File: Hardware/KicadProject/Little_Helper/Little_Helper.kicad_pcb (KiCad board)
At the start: 4 copper layers, 84 x 19.6 mm, 1 part, among them U1 ESP32-S3-MINI-1

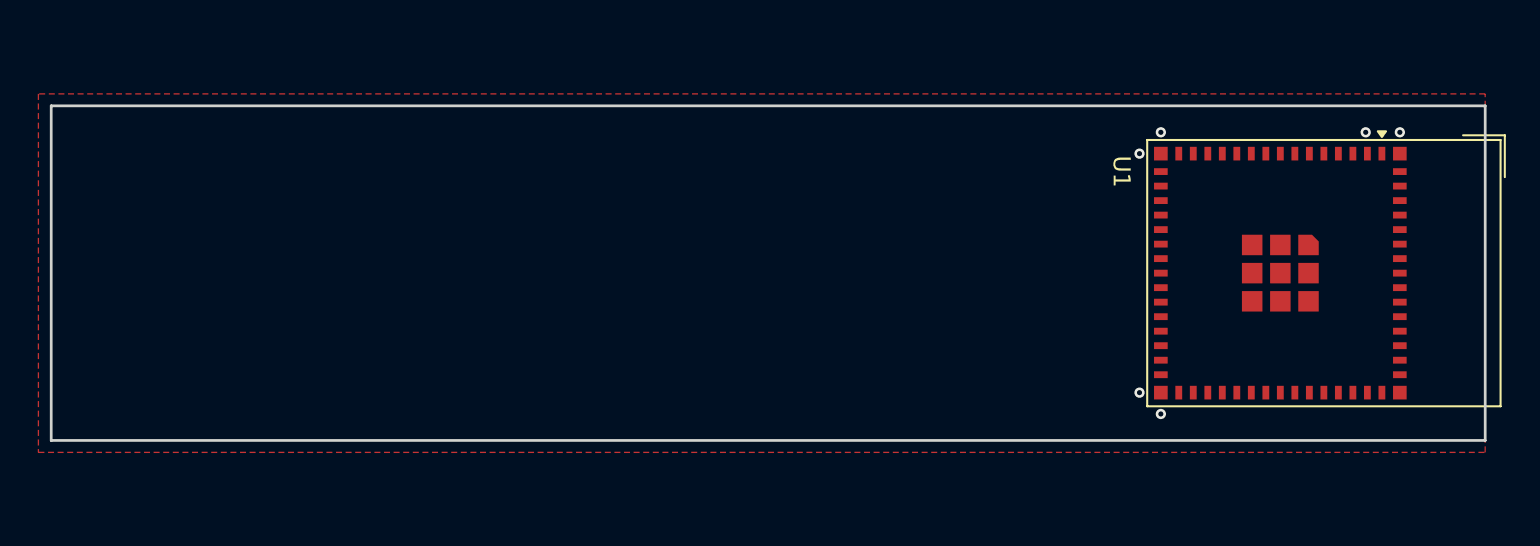
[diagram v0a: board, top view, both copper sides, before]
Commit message: fix some library mismatch
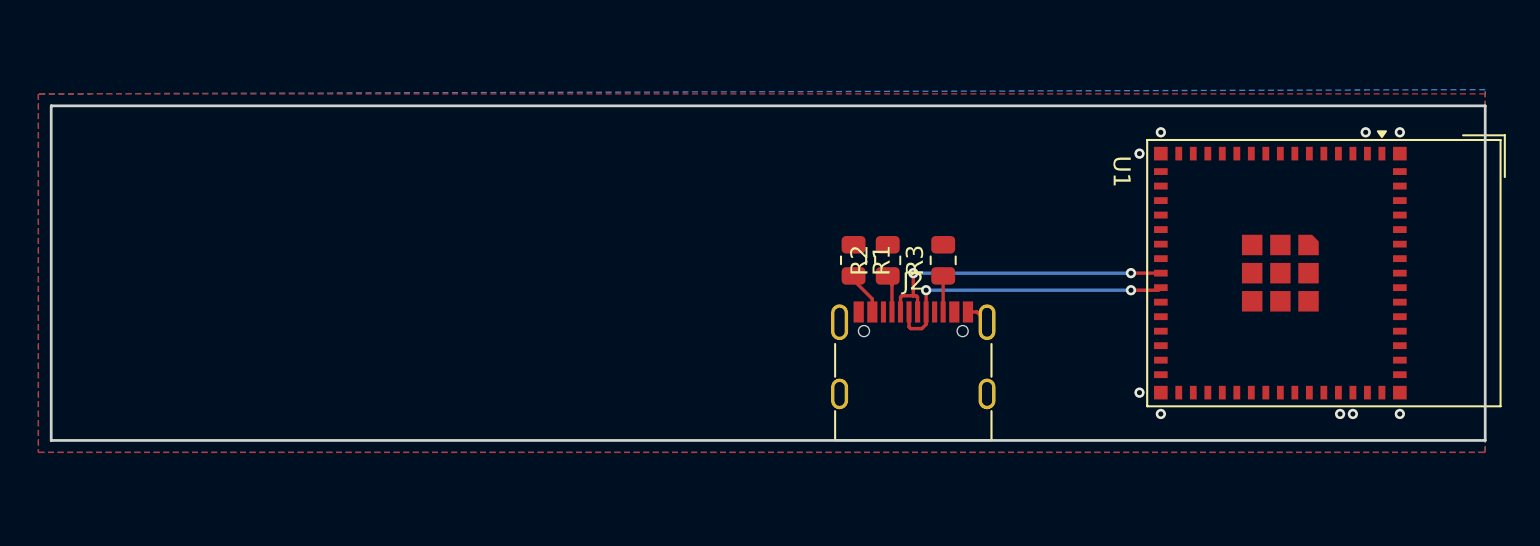
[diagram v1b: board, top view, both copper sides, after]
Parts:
- added J2: USB_C_Receptacle_USB2.0_16P, Connector_USB:USB_C_Receptacle_G-Switch_GT-USB-7010ASV, F.Cu at (8.50, 6.00)
- added R1: 100k, Resistor_SMD:R_0805_2012Metric, F.Cu at (5.00, -0.75)
- added R2: 5k1, Resistor_SMD:R_0805_2012Metric, F.Cu at (7.00, -0.75)
- added R3: 5k1, Resistor_SMD:R_0805_2012Metric, F.Cu at (10.2, -0.75)
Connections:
- U1 pad 23: unconnected-(U1-IO19-Pad23) -> /Usb_D-
- U1 pad 24: unconnected-(U1-IO20-Pad24) -> /Usb_D+
- U1 pad 3: unconnected-(U1-3V3-Pad3) -> +3.3V
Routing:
- net /Usb_D-: track 0.00 -> 18.6 mm, vias 0 -> 2
- net /Usb_D+: track 0.00 -> 17.8 mm, vias 0 -> 2
- net VBUS: track 0.00 -> 2.32 mm
- net Net-(J2-CC2): track 0.00 -> 2.11 mm
- net Net-(J2-CC1): track 0.00 -> 1.97 mm
- net GND: track 0.00 -> 1.37 mm, vias 6 -> 9
- added copper zone on B.Cu, net GND

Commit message: add tactile buttons
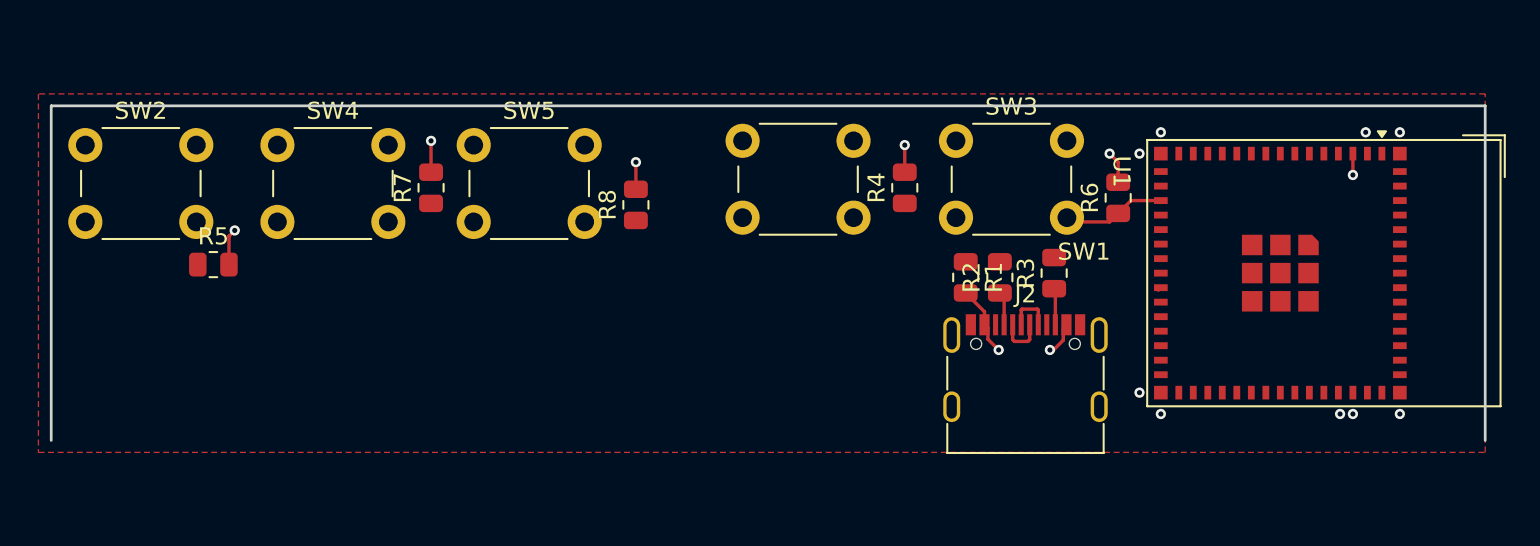
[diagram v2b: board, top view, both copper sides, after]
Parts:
- added R4: 10k, Resistor_SMD:R_0805_2012Metric, F.Cu at (8.00, -5.00)
- added R5: 10k, Resistor_SMD:R_0805_2012Metric, F.Cu at (-32.5, -0.50)
- added R6: 10k, Resistor_SMD:R_0805_2012Metric, F.Cu at (20.5, -4.41)
- added R7: 10k, Resistor_SMD:R_0805_2012Metric, F.Cu at (-19.8, -5.00)
- added R8: 10k, Resistor_SMD:R_0805_2012Metric, F.Cu at (-7.75, -4.00)
- added SW1: SW_Push, Button_Switch_THT:SW_PUSH_6mm_H5mm, F.Cu at (5.00, -3.25)
- added SW2: SW_Push, Button_Switch_THT:SW_PUSH_6mm_H5mm, F.Cu at (-40.0, -7.50)
- added SW3: SW_Push, Button_Switch_THT:SW_PUSH_6mm_H5mm, F.Cu at (11.0, -7.75)
- added SW4: SW_Push, Button_Switch_THT:SW_PUSH_6mm_H5mm, F.Cu at (-28.8, -7.50)
- added SW5: SW_Push, Button_Switch_THT:SW_PUSH_6mm_H5mm, F.Cu at (-17.2, -7.50)
- moved R1 6.65 mm to (11.6, 0.25)
- moved R2 6.65 mm to (13.6, 0.25)
- moved J2 6.61 mm to (15.1, 6.75)
- moved R3 6.54 mm to (16.8, 0.00)
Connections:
- U1 pad 14: unconnected-(U1-IO10-Pad14) -> /BTN_1_RV
- U1 pad 15: unconnected-(U1-IO11-Pad15) -> /BTN_1_STOP
- U1 pad 16: unconnected-(U1-IO12-Pad16) -> /BTN_1_VW
- U1 pad 17: unconnected-(U1-IO13-Pad17) -> /BTN_1_REC
- U1 pad 18: unconnected-(U1-IO14-Pad18) -> /BTN_1_PL
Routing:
- net /Usb_D-: track 18.6 -> 2.83 mm, vias 2 -> 0
- net /Usb_D+: track 17.8 -> 2.99 mm, vias 2 -> 0
- net +3.3V: track 0.00 -> 10.3 mm, vias 0 -> 6
- net /BTN_1_PL: track 0.00 -> 6.41 mm
- net VBUS: track 2.32 -> 6.14 mm, vias 0 -> 2
- net GND: track 1.37 -> 0.00 mm
- added copper zone on In2.Cu, net +3.3V
- added copper zone on In2.Cu, net VBUS
- removed copper zone on B.Cu, net GND

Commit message: board in progress
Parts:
- removed the R3 at (16.8, 0.00)
- added C1: 10uF, Capacitor_SMD:C_0603_1608Metric, F.Cu at (-3.00, -0.10)
- added C2: 10uF, Capacitor_SMD:C_0603_1608Metric, F.Cu at (32.6, -9.60)
- added C3: 10uF, Capacitor_SMD:C_0603_1608Metric, F.Cu at (-7.80, 1.30)
- added C4: 10uF, Capacitor_SMD:C_0603_1608Metric, F.Cu at (-18.1, 7.20)
- added C5: 10uF, Capacitor_SMD:C_0603_1608Metric, F.Cu at (29.4, -9.57)
- added C6: 10uF, Capacitor_SMD:C_0603_1608Metric, F.Cu at (31.0, -9.57)
- added C7: 1uF, Capacitor_SMD:C_0603_1608Metric, F.Cu at (34.2, -9.62)
- added C8: 10uF, Capacitor_SMD:C_0603_1608Metric, F.Cu at (-8.10, 8.40)
- added C9: 1uF, Capacitor_SMD:C_0603_1608Metric, F.Cu at (25.3, 8.80)
- added D1: MBR0540, Diode_SMD:D_0805_2012Metric, F.Cu at (-14.6, 9.60)
- added D2: LED, LED_SMD:LED_0603_1608Metric, F.Cu at (-11.3, 7.00)
- added D3: WS2812B, LED_SMD:LED_WS2812B_PLCC4_5.0x5.0mm_P3.2mm, F.Cu at (-25.1, 2.00)
- added D4: BAS16, ba_sot:sot_23, F.Cu at (-11.7, 0.20)
- added J2: Conn_01x02_Pin, Connector_Hirose:Hirose_DF13-02P-1.25DSA_1x02_P1.25mm_Vertical, B.Cu at (-36.9, 8.30)
- added Q1: DMG3415U, Package_TO_SOT_SMD:SOT-23, F.Cu at (-18.2, 9.90)
- added R10: 5k1, Resistor_SMD:R_0805_2012Metric, F.Cu at (-11.4, 9.10)
- added R11: 5k1, Resistor_SMD:R_0805_2012Metric, F.Cu at (-4.80, 3.70)
- added R9: 10k, Resistor_SMD:R_0805_2012Metric, F.Cu at (20.5, -4.50)
- added SW6: SW_SPST, Button_Switch_SMD:SW_SPDT_CK_JS102011SAQN, F.Cu at (-26.2, 10.6)
- added SW7: SW_Push, Button_Switch_SMD:SW_Push_1P1T_NO_Vertical_Wuerth_434133025816, F.Cu at (16.5, 7.90)
- added SW8: SW_Push, Button_Switch_SMD:SW_Push_1P1T_NO_Vertical_Wuerth_434133025816, F.Cu at (16.4, 3.70)
- added U1: AP2112K-3.3, Package_TO_SOT_SMD:SOT-23-5, F.Cu at (-11.6, 3.80)
- added U3: MCP73831-2-OT, Package_TO_SOT_SMD:SOT-23-5, F.Cu at (-5.20, 7.60)
- J1: renamed from J2; value USB_C_Receptacle_USB2.0_16P -> USB_B_Micro; footprint Connector_USB:USB_C_Receptacle_G-Switch_GT-USB-7010ASV -> Connector_USB:USB_Micro-B_Wuerth_629105150521_CircularHoles
- R3: renamed from R1; value 100k -> R2012_100K; footprint Resistor_SMD:R_0805_2012Metric -> ba_res:r2012
- R4: value 10k -> 100k
- moved SW1 45.2 mm to (-40.0, -7.75), turned to 0 degrees
- moved R6 40.0 mm to (-19.5, -5.34)
- moved SW5 28.3 mm to (11.0, -7.75)
- moved SW3 28.0 mm to (-17.0, -7.75)
- moved SW4 27.3 mm to (-1.50, -7.75)
- moved R4 24.6 mm to (-15.0, 3.80)
- moved R8 15.8 mm to (8.00, -5.00)
- moved R7 12.0 mm to (-7.75, -4.25)
- moved SW2 11.5 mm to (-28.5, -7.75)
- moved R1 10.6 mm to (20.7, 8.09), turned to -90 degrees
- moved J1 7.98 mm to (7.39, 8.95)
- moved R3 5.99 mm to (6.60, 3.60), turned to 90 degrees
- renumbered R2 to R1, U1 to U2
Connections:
- R1 pad 1: Net-(J2-CC1) -> +3.3V
- R1 pad 2: GND -> /RESET
- R3 pad 1: GND -> VBUS
- R3 pad 2: VBUS -> GND
- R4 pad 1: /BTN_1_REC -> Net-(U1-EN)
- R4 pad 2: +3.3V -> /NEOPIX_VDD
- R6 pad 1: /BTN_1_PL -> /BTN_1_STOP
- R7 pad 1: /BTN_1_STOP -> /BTN_1_VW
- R8 pad 1: /BTN_1_VW -> /BTN_1_REC
- SW1 pad 2: /BTN_1_REC -> /BTN_1_RV
- SW2 pad 2: /BTN_1_RV -> /BTN_1_STOP
- SW3 pad 2: /BTN_1_PL -> /BTN_1_VW
- SW4 pad 2: /BTN_1_STOP -> /BTN_1_REC
- SW5 pad 2: /BTN_1_VW -> /BTN_1_PL
- U2 pad 28: unconnected-(U1-IO33-Pad28) -> /NEOPIX
- U2 pad 4: unconnected-(U1-IO0-Pad4) -> /BOOT0
- U2 pad 45: unconnected-(U1-EN-Pad45) -> /RESET
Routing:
- net GND: track 0.00 -> 158.8 mm, vias 9 -> 31
- net /BTN_1_RV: track 0.00 -> 76.9 mm, vias 0 -> 2
- net /BTN_1_STOP: track 0.00 -> 56.4 mm, vias 0 -> 2
- net /NEOPIX: track 0.00 -> 50.8 mm, vias 0 -> 2
- net /BTN_1_VW: track 0.00 -> 45.1 mm, vias 0 -> 2
- net +3.3V: track 10.3 -> 45.8 mm, vias 6 -> 10
- net /BOOT0: track 0.00 -> 31.0 mm, vias 0 -> 2
- net /NEOPIX_VDD: track 0.00 -> 28.8 mm
- net /BTN_1_REC: track 0.00 -> 28.3 mm, vias 0 -> 2
- net /RESET: track 0.00 -> 24.3 mm
- net VBUS: track 6.14 -> 25.2 mm
- net /Usb_D-: track 2.83 -> 20.8 mm, vias 0 -> 2
- net /Usb_D+: track 2.99 -> 19.0 mm, vias 0 -> 2
- net Net-(J2-Pin_2): track 0.00 -> 11.7 mm
- net +BATT: track 0.00 -> 9.66 mm, vias 0 -> 3
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- added copper zone on In2.Cu, net +BATT
- added copper zone on B.Cu, net GND
- removed copper zone on F.Cu, net GND
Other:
- board size 84 x 19.6 mm -> 84 x 25.6 mm
- rule pad_to_mask_clearance: 0 -> 0.05

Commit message: some changes on pads
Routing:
- added copper zone on F.Cu, net GND

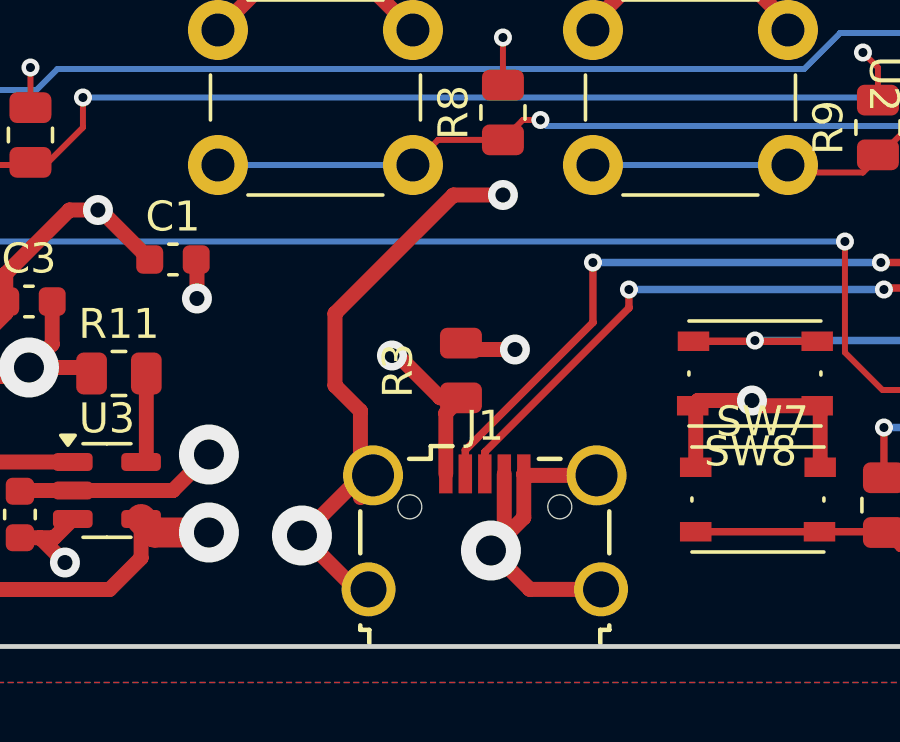
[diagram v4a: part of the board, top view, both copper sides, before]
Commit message: change usb micro connector
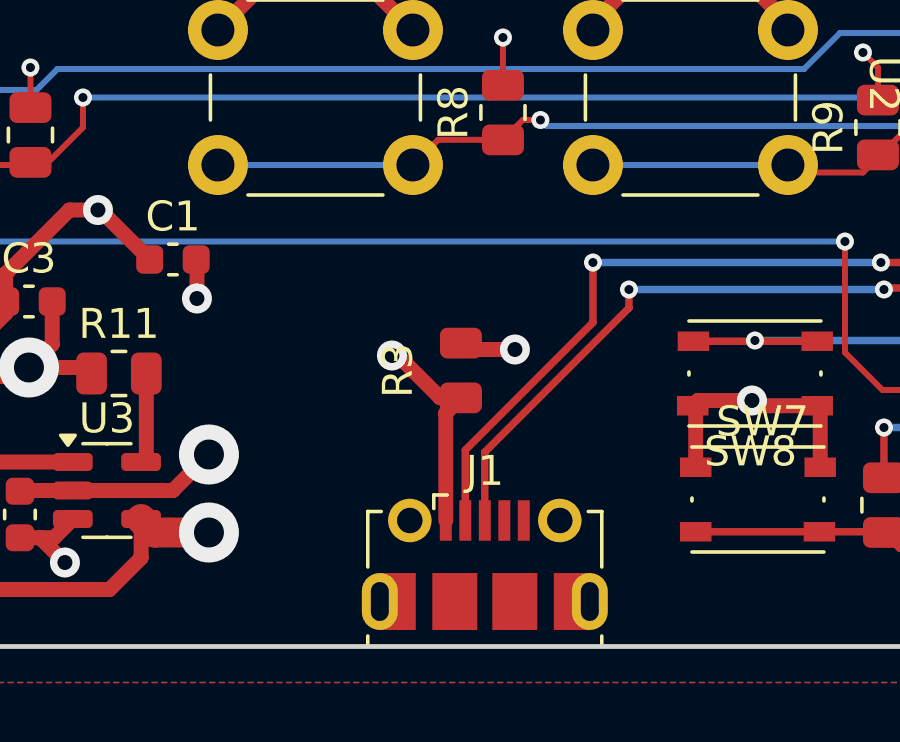
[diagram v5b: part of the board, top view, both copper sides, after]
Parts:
- J1: value USB_B_Micro -> USB_B_Micro_Molex_1050171001_JLCPCB_C505111; footprint Connector_USB:USB_Micro-B_Wuerth_629105150521_CircularHoles -> Connector_USB:USB_Micro-B_Molex-105017-0001
- moved J1 1.12 mm to (7.39, 10.1)
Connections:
- J1 pad 4: GND -> unconnected-(J1-ID-Pad4)
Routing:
- net GND: track 158.8 -> 126.5 mm, vias 31 -> 28
- net VBUS: track 25.2 -> 26.7 mm
- net /Usb_D-: track 20.8 -> 22.4 mm
- net /Usb_D+: track 19.0 -> 20.5 mm

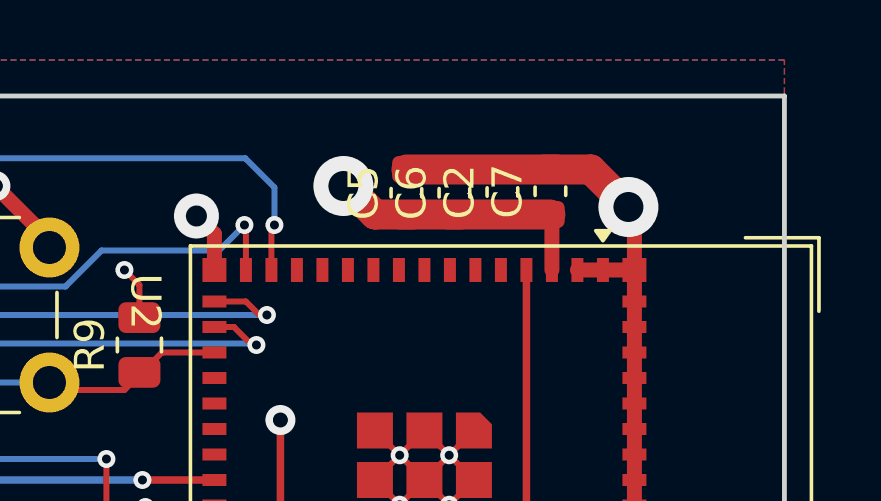
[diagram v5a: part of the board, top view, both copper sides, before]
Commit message: 10uf cap from 0603 to 0805
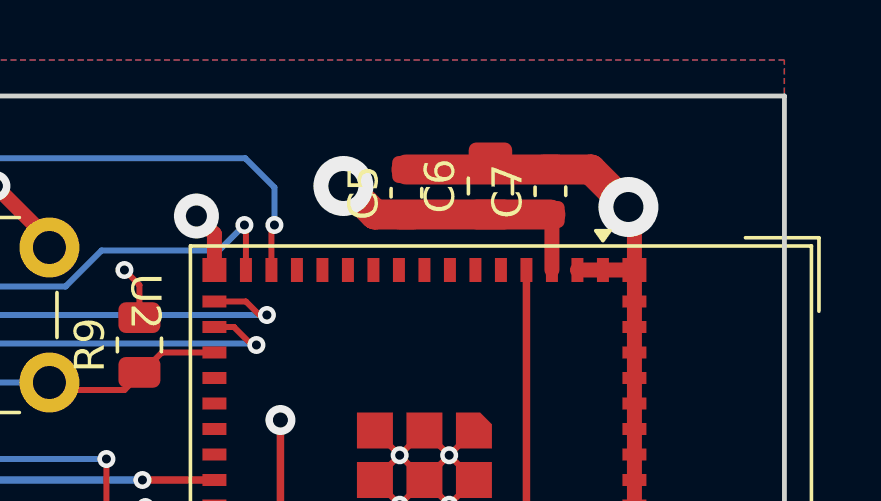
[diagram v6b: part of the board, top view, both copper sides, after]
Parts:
- removed C2: 10uF, Capacitor_SMD:C_0603_1608Metric
- C6: footprint Capacitor_SMD:C_0603_1608Metric -> Capacitor_SMD:C_0805_2012Metric
- moved C6 1.22 mm to (32.2, -9.80)

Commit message: save prev changes
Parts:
- C1, C3, C4, C5, C8: footprint Capacitor_SMD:C_0603_1608Metric -> Capacitor_SMD:C_0805_2012Metric
- moved C5 0.93 mm to (30.3, -9.80)
- moved C8 0.28 mm to (-8.30, 8.60)
- moved C6 0.20 mm to (32.4, -9.80)
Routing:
- net +3.3V: track 45.8 -> 44.8 mm
- net +BATT: track 9.66 -> 10.5 mm
- net GND: track 126.5 -> 125.8 mm

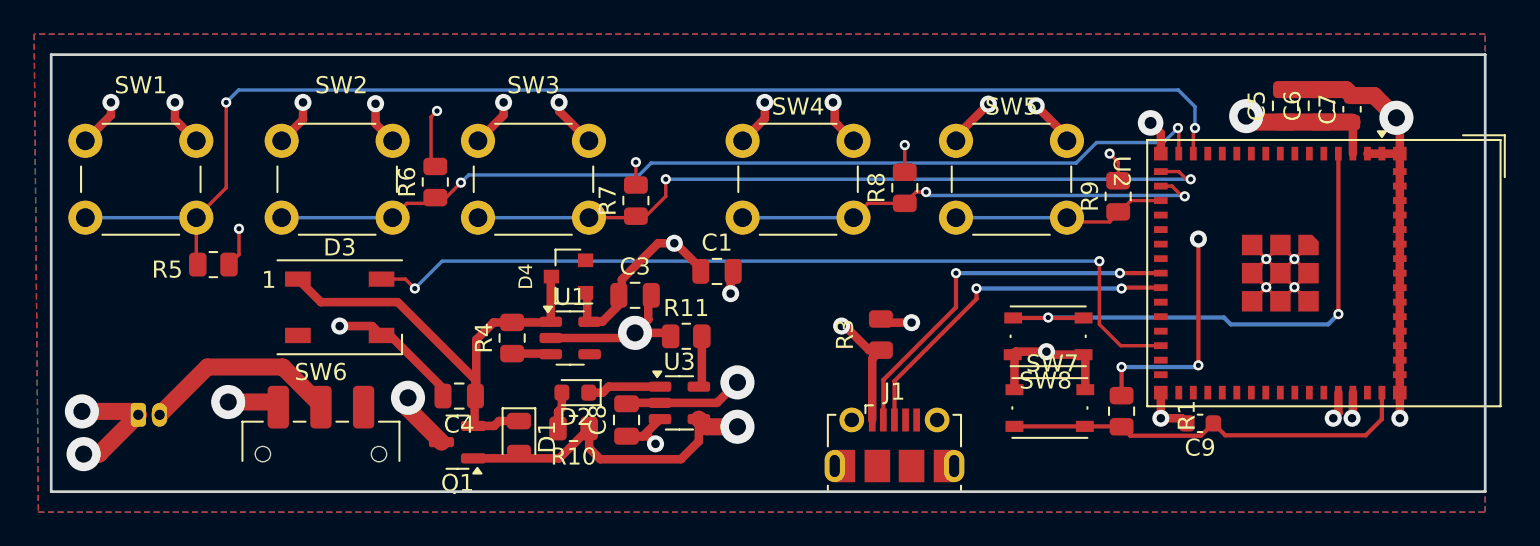
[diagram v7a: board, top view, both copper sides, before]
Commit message: select the right footprint
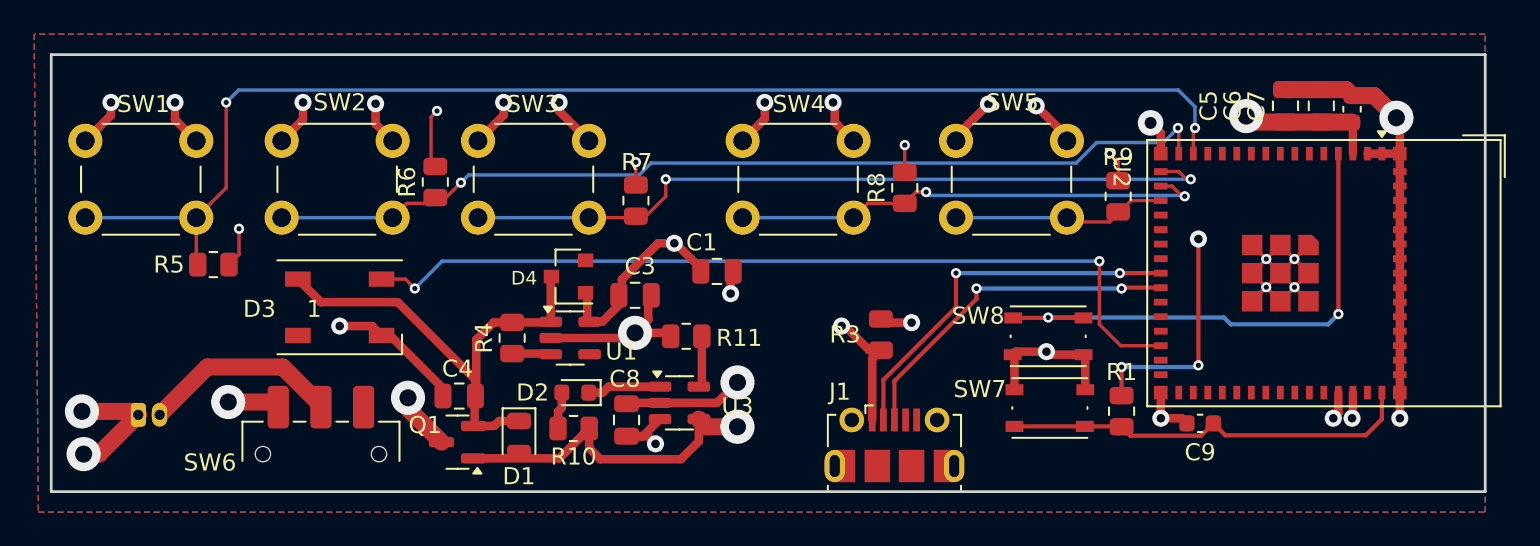
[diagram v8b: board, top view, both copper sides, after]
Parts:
- R1: value 5k1 -> 10k
